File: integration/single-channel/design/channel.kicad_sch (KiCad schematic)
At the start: 48 parts, among them J1 MCX edge jack 50R, J2 MCX edge jack 50R, J3 MCX edge jack 50R, J4 MCX edge jack 50R, J5 Screw terminal 3-pos 5.08mm, U1 CR-112, U2 CR-200-1us, U3 CR-210, U4 THS3491

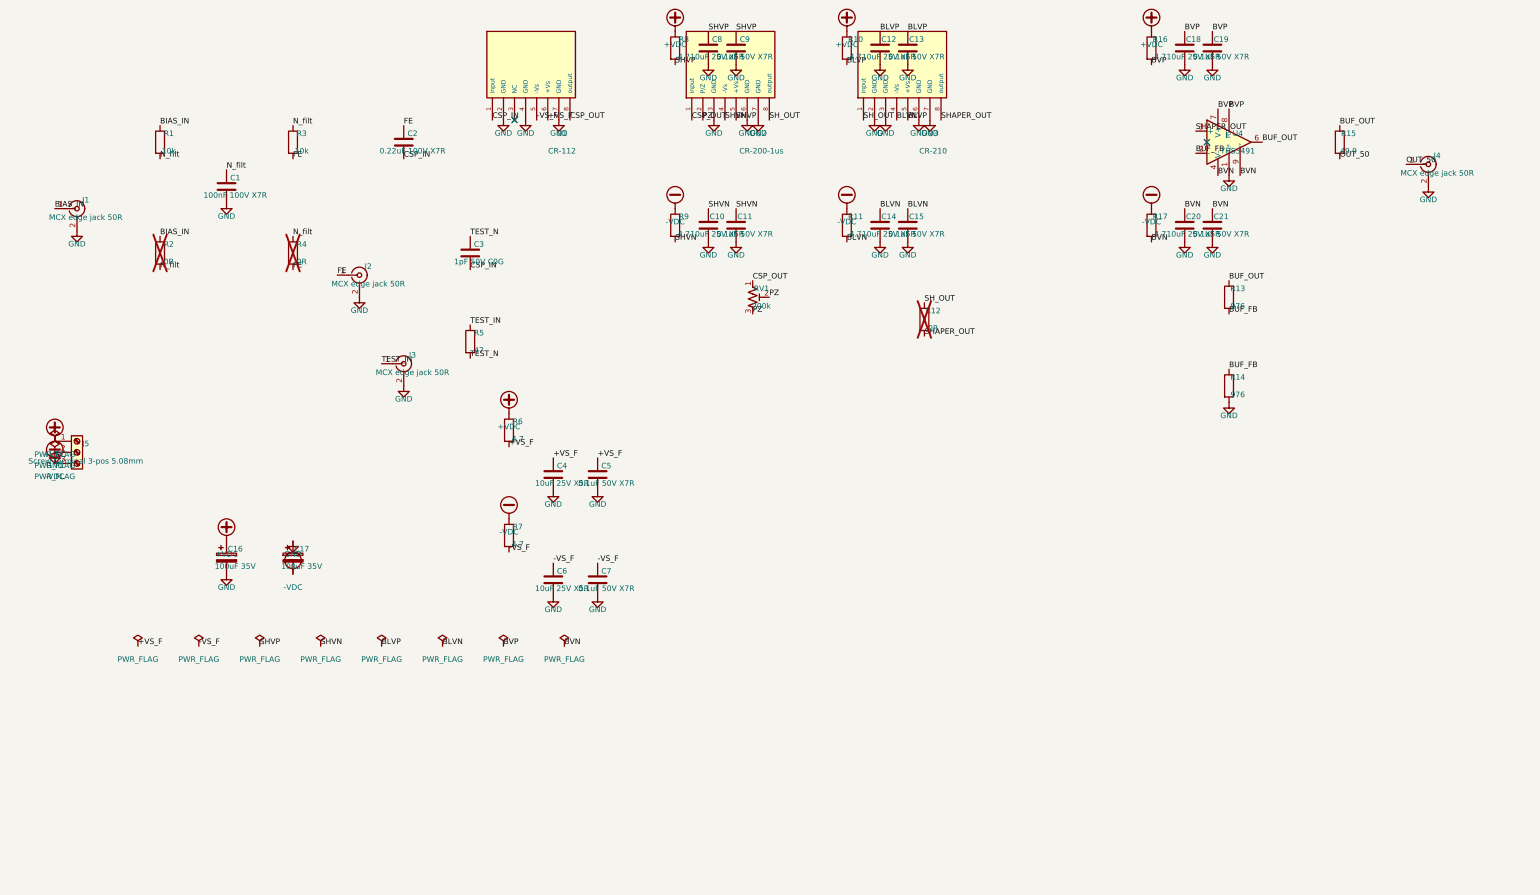
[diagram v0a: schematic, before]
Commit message: Single-channel: 2026-07 rework + rail reverse-polarity protection + doc reconcile
Rail protection (per rail): screw terminal -> PTC (F1/F2, Littelfuse 1206L010/60WR)
-> series Schottky (D1/D2, onsemi SS14) -> board rail. Blocks reversed supply leads and
interrupts sustained faults. No over-voltage clamp: the +/-13 V Cremat module supply
abs-max vs the +/-12 V nominal rail leaves no passive-clamp window (datasheet-verified,
adversarially checked), so over-voltage is an operational limit. New nets
+VDC_IN/+VDC_F/-VDC_IN/-VDC_F.

Folds in the prior 2026-07 design rework:
- Output buffer is now populate-or-bypass: THS3491 block DNP by default + JP_BUF 0R bypass
  (default build = CR-210 drives the 49.9 back-term directly, OUT_50 = 1/2 * SHAPER_OUT).
- Test input reworked to a coax-terminated injector: R5 = 47R shunt to GND, C3 = 1pF into
  CSP_IN; net TEST_N removed.
- Per-rail decoupling reduced to 4.7R + 10uF (the 0.1uF HF caps dropped board-wide).
- channel.kicad_sch redrawn as a human-review WIRED layout.
- Sourcing (2026-07-07 sweep): Cf NRND -> CL21B104KCFNNNE; Digi-Key PN fixes; 10uF 25V bulk
  flagged Active-but-0-stock (16-wk lead), Taiyo Yuden alt noted.

BOM: 45 refs / 20 distinct MPNs (added 4 protection rows; fixed the R_test description).
Schematic ERC 0/0.

Docs reconciled to the reworked design (INTERFACE.md, SESSION_REPORT.md, SESSION_LOG.md);
an adversarial doc-vs-design audit returned CLEAN.

NOTE: channel.kicad_pcb is STALE (predates this rework) -- the PCB layout rebuild is next.
Also includes incidental KiCad project-file (.kicad_pro) boilerplate updates in
hardware/, final-board/, chips-board/ from opening those projects.

Co-Authored-By: Claude Opus 4.8 <noreply@anthropic.com>
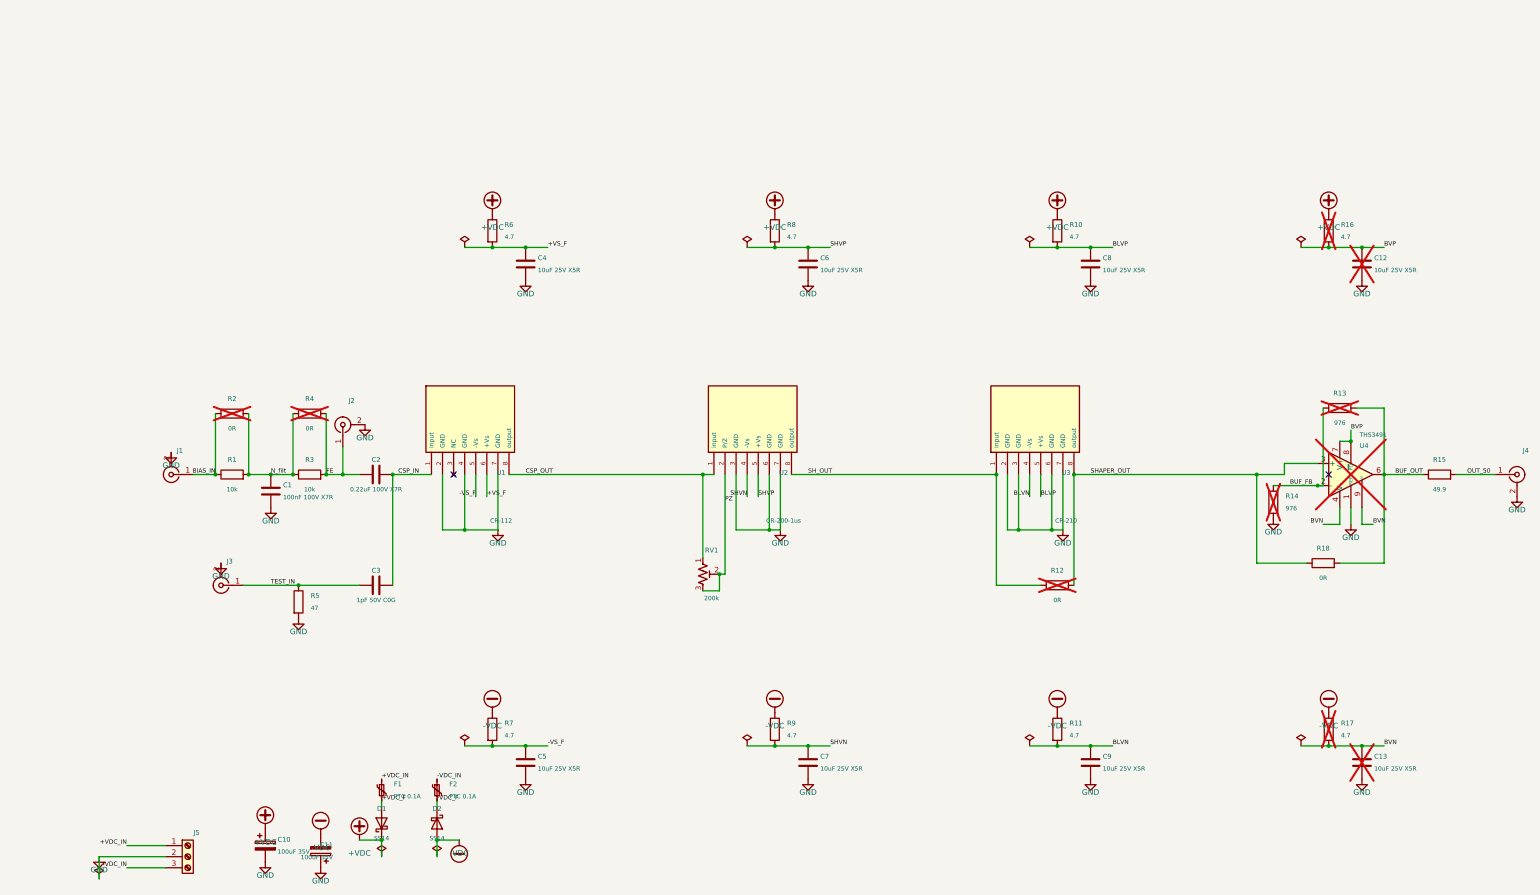
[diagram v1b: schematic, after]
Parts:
- removed C11, C13, C15, C19, C21, C5, C7, C9: 0.1uF 50V X7R, Capacitor_SMD:C_0805_2012Metric, symbol Device:C
- added D1, D2: SS14, Diode_SMD:D_SMA, symbol Device:D_Schottky
- added F1, F2: PTC 0.1A, Fuse:Fuse_1206_3216Metric, symbol Device:Polyfuse_Small
- added R18: 0R, Resistor_SMD:R_0805_2012Metric, symbol Device:R
- C1: Distributor PN 1276-2447-1-ND -> 1276-6840-1-ND; MPN CL21B104KCC5PNC -> CL21B104KCFNNNE
- C12: renamed from C18; Distributor PN 1276-1037-1-ND -> 1276-2891-1-ND; now not fitted
- C13: renamed from C20; Distributor PN 1276-1037-1-ND -> 1276-2891-1-ND; now not fitted
- C2: Distributor PN 490-GRM21AR72A224KAC5K -> 490-8306-1-ND
- C3: Distributor PN 311-CC0805CRNPO9BN1R0CT-ND -> 311-1089-1-ND
- C4: Distributor PN 1276-1037-1-ND -> 1276-2891-1-ND
- C5: renamed from C6; Distributor PN 1276-1037-1-ND -> 1276-2891-1-ND
- C6: renamed from C8; Distributor PN 1276-1037-1-ND -> 1276-2891-1-ND
- C7: renamed from C10; Distributor PN 1276-1037-1-ND -> 1276-2891-1-ND
- C8: renamed from C12; Distributor PN 1276-1037-1-ND -> 1276-2891-1-ND
- C9: renamed from C14; Distributor PN 1276-1037-1-ND -> 1276-2891-1-ND
- R13, R14, R16, R17, U4: now not fitted
- renumbered C16 to C10, C17 to C11
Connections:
- net +VDC: now also D1.1 (K); no longer J5.1 (Pin_1)
- net -VDC: now also D2.2 (A); no longer J5.3 (Pin_3)
- net BUF_OUT: now also R18.2
- net GND: now also R5.2
- net SHAPER_OUT: now also R18.1
- net TEST_IN: now also C3.1
- removed net TEST_N: C3.1, R5.2
- new net +VDC_F: D1.2 (A), F1.2
- new net +VDC_IN: F1.1, J5.1 (Pin_1)
- new net -VDC_F: D2.1 (K), F2.2
- new net -VDC_IN: F2.1, J5.3 (Pin_3)
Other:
- moved on the sheet: C1, C10, C11, C2, C3, C4, C5, C6, C7, C8, C9, J1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

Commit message: Sourcing: swap 10uF bulk to in-stock KEMET C0805C106K3PACTU
The fitted 10uF 25V X5R 0805 bulk (x8 decoupling caps) was the 0-stock Samsung
CL21A106KAYNNNE (Active, 29-wk lead). Swapped to the in-stock KEMET C0805C106K3PACTU
(DK 399-11939-1-ND) - re-verified live: ~255k stock, Active, $0.23 q1 / $0.083 q100,
exact 0805 drop-in. Beat Taiyo Yuden (in stock but ~600 pcs), TDK (stocked but NRND),
Murata/Yageo (0-stock). Samsung kept as documented alternate (same-mfr fallback
CL21A106KACLRNC ~71k). Value-only swap in gen_sch.py (8 caps) + 8 BOM rows; 0805 footprint
and PCB unchanged; schematic ERC 0/0. Docs updated (INTERFACE, SESSION_REPORT/LOG, sourcing).

Co-Authored-By: Claude Opus 4.8 <noreply@anthropic.com>
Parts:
- C12, C13, C4, C5, C6, C7, C8, C9: Distributor PN 1276-2891-1-ND -> 399-11939-1-ND; MPN CL21A106KAYNNNE -> C0805C106K3PACTU; Manufacturer Samsung Electro-Mechanics -> KEMET
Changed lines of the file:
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@@
 			(effects (font (size 1.27 1.27)))
 		)
-		(property "MPN" "CL21A106KAYNNNE"
+		(property "MPN" "C0805C106K3PACTU"
 			(at 128.27 67.31 0)
 			(hide yes)
 			(effects (font (size 1.27 1.27)))
 		)
-		(property "Manufacturer" "Samsung Electro-Mechanics"
+		(property "Manufacturer" "KEMET"
 			(at 128.27 67.31 0)
 			(hide yes)
 			(effects (font (size 1.27 1.27)))
 		)
-		(property "Distributor PN" "1276-2891-1-ND"
+		(property "Distributor PN" "399-11939-1-ND"
 			(at 128.27 67.31 0)
 			(hide yes)
@@
 			(effects (font (size 1.27 1.27)))
 		)
-		(property "MPN" "CL21A106KAYNNNE"
+		(property "MPN" "C0805C106K3PACTU"
 			(at 128.27 181.61 0)
 			(hide yes)
 			(effects (font (size 1.27 1.27)))
 		)
-		(property "Manufacturer" "Samsung Electro-Mechanics"
+		(property "Manufacturer" "KEMET"
 			(at 128.27 181.61 0)
 			(hide yes)
 			(effects (font (size 1.27 1.27)))
 		)
-		(property "Distributor PN" "1276-2891-1-ND"
+		(property "Distributor PN" "399-11939-1-ND"
 			(at 128.27 181.61 0)
 			(hide yes)
@@
 			(effects (font (size 1.27 1.27)))
 		)
-		(property "MPN" "CL21A106KAYNNNE"
+		(property "MPN" "C0805C106K3PACTU"
 			(at 193.04 67.31 0)
 			(hide yes)
 			(effects (font (size 1.27 1.27)))
 		)
-		(property "Manufacturer" "Samsung Electro-Mechanics"
+		(property "Manufacturer" "KEMET"
 			(at 193.04 67.31 0)
 			(hide yes)
 			(effects (font (size 1.27 1.27)))
 		)
-		(property "Distributor PN" "1276-2891-1-ND"
+		(property "Distributor PN" "399-11939-1-ND"
 			(at 193.04 67.31 0)
 			(hide yes)
@@
 			(effects (font (size 1.27 1.27)))
 		)
-		(property "MPN" "CL21A106KAYNNNE"
+		(property "MPN" "C0805C106K3PACTU"
 			(at 193.04 181.61 0)
 			(hide yes)
 			(effects (font (size 1.27 1.27)))
 		)
-		(property "Manufacturer" "Samsung Electro-Mechanics"
+		(property "Manufacturer" "KEMET"
 			(at 193.04 181.61 0)
 			(hide yes)
 			(effects (font (size 1.27 1.27)))
 		)
-		(property "Distributor PN" "1276-2891-1-ND"
+		(property "Distributor PN" "399-11939-1-ND"
 			(at 193.04 181.61 0)
 			(hide yes)
@@
 			(effects (font (size 1.27 1.27)))
 		)
-		(property "MPN" "CL21A106KAYNNNE"
+		(property "MPN" "C0805C106K3PACTU"
 			(at 257.81 67.31 0)
 			(hide yes)
 			(effects (font (size 1.27 1.27)))
 		)
-		(property "Manufacturer" "Samsung Electro-Mechanics"
+		(property "Manufacturer" "KEMET"
 			(at 257.81 67.31 0)
 			(hide yes)
 			(effects (font (size 1.27 1.27)))
 		)
-		(property "Distributor PN" "1276-2891-1-ND"
+		(property "Distributor PN" "399-11939-1-ND"
 			(at 257.81 67.31 0)
 			(hide yes)
@@
 			(effects (font (size 1.27 1.27)))
 		)
-		(property "MPN" "CL21A106KAYNNNE"
+		(property "MPN" "C0805C106K3PACTU"
 			(at 257.81 181.61 0)
 			(hide yes)
 			(effects (font (size 1.27 1.27)))
 		)
-		(property "Manufacturer" "Samsung Electro-Mechanics"
+		(property "Manufacturer" "KEMET"
 			(at 257.81 181.61 0)
 			(hide yes)
 			(effects (font (size 1.27 1.27)))
 		)
-		(property "Distributor PN" "1276-2891-1-ND"
+		(property "Distributor PN" "399-11939-1-ND"
 			(at 257.81 181.61 0)
 			(hide yes)
@@
 			(effects (font (size 1.27 1.27)))
 		)
-		(property "MPN" "CL21A106KAYNNNE"
+		(property "MPN" "C0805C106K3PACTU"
 			(at 320.04 67.31 0)
 			(hide yes)
 			(effects (font (size 1.27 1.27)))
 		)
-		(property "Manufacturer" "Samsung Electro-Mechanics"
+		(property "Manufacturer" "KEMET"
 			(at 320.04 67.31 0)
 			(hide yes)
 			(effects (font (size 1.27 1.27)))
 		)
-		(property "Distributor PN" "1276-2891-1-ND"
+		(property "Distributor PN" "399-11939-1-ND"
 			(at 320.04 67.31 0)
 			(hide yes)
@@
 			(effects (font (size 1.27 1.27)))
 		)
-		(property "MPN" "CL21A106KAYNNNE"
+		(property "MPN" "C0805C106K3PACTU"
 			(at 320.04 181.61 0)
 			(hide yes)
 			(effects (font (size 1.27 1.27)))
 		)
-		(property "Manufacturer" "Samsung Electro-Mechanics"
+		(property "Manufacturer" "KEMET"
 			(at 320.04 181.61 0)
 			(hide yes)
 			(effects (font (size 1.27 1.27)))
 		)
-		(property "Distributor PN" "1276-2891-1-ND"
+		(property "Distributor PN" "399-11939-1-ND"
 			(at 320.04 181.61 0)
 			(hide yes)

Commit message: single-channel: edge-mount MCX (user's Linx CONMCX013-T footprint) + connector orientation fixes
- Swap MCX to the user-downloaded cremat:MCX_CONMCX013-T (shield tabs G1/G2 -> pad 2 so
  GND connects via Conn_Coaxial pin 2; trimmed the connector-tiling edge-extension
  Edge.Cuts segments). Update gen_sch FP_MCX + gen_pcb .kicad_dru condition.
- MCX 3D model rotate (xyz 270 0 0): coax mating face now points OFF the board edge
  (raw STEP had it vertical/up). 3D-cosmetic patch to the routed board, no reroute.
- Fix the MCX edge-notch generator: place jacks by footprint origin (rot 90/270), outline
  cuts the notch read back from each placed MCX, demote footprint Edge.Cuts -> Dwgs.User,
  keep cremat: FPID prefix; write_dru() waives edge_clearance for the shield tabs.
- J5 screw terminal rot 0 -> 180 so the wire funnels face the top edge (was inward).
- Re-autorouted (FreeRouting / Java 25, dead-proxy headless recipe in docs/FREEROUTING.md):
  DRC 0 errors / 0 unconnected (4 benign lib_footprint_mismatch from the Edge.Cuts demotion).
- ERC 0; netlist membership identical to baseline (footprint field only, circuit unchanged).
- Add docs/HARDWARE_DEV_PLAYBOOK.md; SESSION_LOG records the ${KIPRJMOD} 3D-render gotcha.

Co-Authored-By: Claude Opus 4.8 <noreply@anthropic.com>
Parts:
- J1, J2, J3, J4: footprint cremat:MCX_CONMCX013_EdgeMount -> cremat:MCX_CONMCX013-T
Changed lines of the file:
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@@
 			(effects (font (size 1.0 1.0)))
 		)
-		(property "Footprint" "cremat:MCX_CONMCX013_EdgeMount"
+		(property "Footprint" "cremat:MCX_CONMCX013-T"
 			(at 46.99 115.57 0)
 			(hide yes)
@@
 			(effects (font (size 1.0 1.0)))
 		)
-		(property "Footprint" "cremat:MCX_CONMCX013_EdgeMount"
+		(property "Footprint" "cremat:MCX_CONMCX013-T"
 			(at 86.36 104.14 0)
 			(hide yes)
@@
 			(effects (font (size 1.0 1.0)))
 		)
-		(property "Footprint" "cremat:MCX_CONMCX013_EdgeMount"
+		(property "Footprint" "cremat:MCX_CONMCX013-T"
 			(at 58.42 140.97 0)
 			(hide yes)
@@
 			(effects (font (size 1.0 1.0)))
 		)
-		(property "Footprint" "cremat:MCX_CONMCX013_EdgeMount"
+		(property "Footprint" "cremat:MCX_CONMCX013-T"
 			(at 355.6 115.57 0)
 			(hide yes)

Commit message: 12ch order-ready v2: socketed Cremat modules, HV-DRC fix, 1U slot-through, JLC+DigiKey ordering package
Four workstreams, all gated (ERC 0 / netlist membership identical / DRC 0 errors,
0 unconnected, 0 parity with hv_bias verified live / renders checked):

SIP-8 sockets (never solder the modules):
- All 36 module sites -> stock PinSocket_1x08 footprint (pad+courtyard identical to the
  old header placeholder). Part: Samtec SS-108-TT-2 (DK 612-SS-108-TT-2-ND) - Cremat's
  own eval-board socket; accepts the modules' 0.51x0.25mm flat pins (live-verified).
  Alt: Harwin D01-9970842. NOT Mill-Max/Preci-Dip 801 (0.7-0.9mm pins).

hv_bias 0.6mm DRC rule was silently disabled - found and fixed at the source:
- Single-channel netclass patterns 'FE'/'N_filt' lacked the leading slash and matched
  nothing -> the 07-11 reroute packed the SiPM-bias front-end at 0.2mm. Patterns now
  '*/'-prefixed; single channel re-routed with the HV rule live in the DSN; 12ch re-tiled.
- A KiCad GUI save flattened twelve-channel.kicad_pro netclasses TWICE (DRC passed
  vacuously). Pipeline now self-heals: gen_pcb re-asserts build_pro() after SaveBoard;
  fill_zones refuses to fill blind (restores netclasses + loud warning).

Enclosure: 2U -> 1U, one board per case, slot-through panels:
- Hammond RM1U1908VBK (vented; ~13W under a 40mm lid). Factory-drawing-verified:
  internal 196.85 depth x 40.09 height; socketed module stack ~32mm -> fits.
- Board W 180 -> 213.2mm: passes through a ~340x7mm milled slot in each front/rear
  panel, protruding 5mm; MCX faces ~8.6mm proud, snap-on fully in the open. Slot
  machining spec in design/SESSION_LOG.md session 14.

Ordering (ORDERING.md = master buy sheet):
- JLCPCB fab + Economic SMT assembly (live-verified incl. wizard quote: ~$74/5 boards
  HASL, large-size fee $5; Economic tier OK, edge notches OK). Package in design/fab/jlc:
  gerber zip + JLC BOM (12 lines, LCSC C-numbers, 8 Basic / 4 Extended) + CPL (246
  FIT-SMD placements). Subs documented: 10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
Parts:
- C2: Distributor PN 490-8306-1-ND -> 399-C0805C224K1RACTUCT-ND; MPN GRM21AR72A224KAC5K -> C0805C224K1RACTU; Manufacturer Murata Electronics -> KEMET
- U1, U2, U3: footprint Connector_PinHeader_2.54mm:PinHeader_1x08_P2.54mm_Vertical -> Connector_PinSocket_2.54mm:PinSocket_1x08_P2.54mm_Vertical
- U4: Distributor PN 296-49085-2-ND -> 296-49085-1-ND
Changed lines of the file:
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@@
 			(effects (font (size 1.27 1.27)))
 		)
-		(property "MPN" "GRM21AR72A224KAC5K"
+		(property "MPN" "C0805C224K1RACTU"
 			(at 93.98 115.57 0)
 			(hide yes)
 			(effects (font (size 1.27 1.27)))
 		)
-		(property "Manufacturer" "Murata Electronics"
+		(property "Manufacturer" "KEMET"
 			(at 93.98 115.57 0)
 			(hide yes)
 			(effects (font (size 1.27 1.27)))
 		)
-		(property "Distributor PN" "490-8306-1-ND"
+		(property "Distributor PN" "399-C0805C224K1RACTUCT-ND"
 			(at 93.98 115.57 0)
 			(hide yes)
@@
 			(effects (font (size 1.0 1.0)))
 		)
-		(property "Footprint" "Connector_PinHeader_2.54mm:PinHeader_1x08_P2.54mm_Vertical"
+		(property "Footprint" "Connector_PinSocket_2.54mm:PinSocket_1x08_P2.54mm_Vertical"
 			(at 120.65 120.65 0)
 			(hide yes)
@@
 			(effects (font (size 1.0 1.0)))
 		)
-		(property "Footprint" "Connector_PinHeader_2.54mm:PinHeader_1x08_P2.54mm_Vertical"
+		(property "Footprint" "Connector_PinSocket_2.54mm:PinSocket_1x08_P2.54mm_Vertical"
 			(at 185.42 120.65 0)
 			(hide yes)
@@
 			(effects (font (size 1.0 1.0)))
 		)
-		(property "Footprint" "Connector_PinHeader_2.54mm:PinHeader_1x08_P2.54mm_Vertical"
+		(property "Footprint" "Connector_PinSocket_2.54mm:PinSocket_1x08_P2.54mm_Vertical"
 			(at 250.19 120.65 0)
 			(hide yes)
@@
 			(effects (font (size 1.27 1.27)))
 		)
-		(property "Distributor PN" "296-49085-2-ND"
+		(property "Distributor PN" "296-49085-1-ND"
 			(at 317.5 115.57 0)
 			(hide yes)
